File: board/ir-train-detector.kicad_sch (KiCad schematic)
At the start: 21 parts, among them J1 Conn_01x03

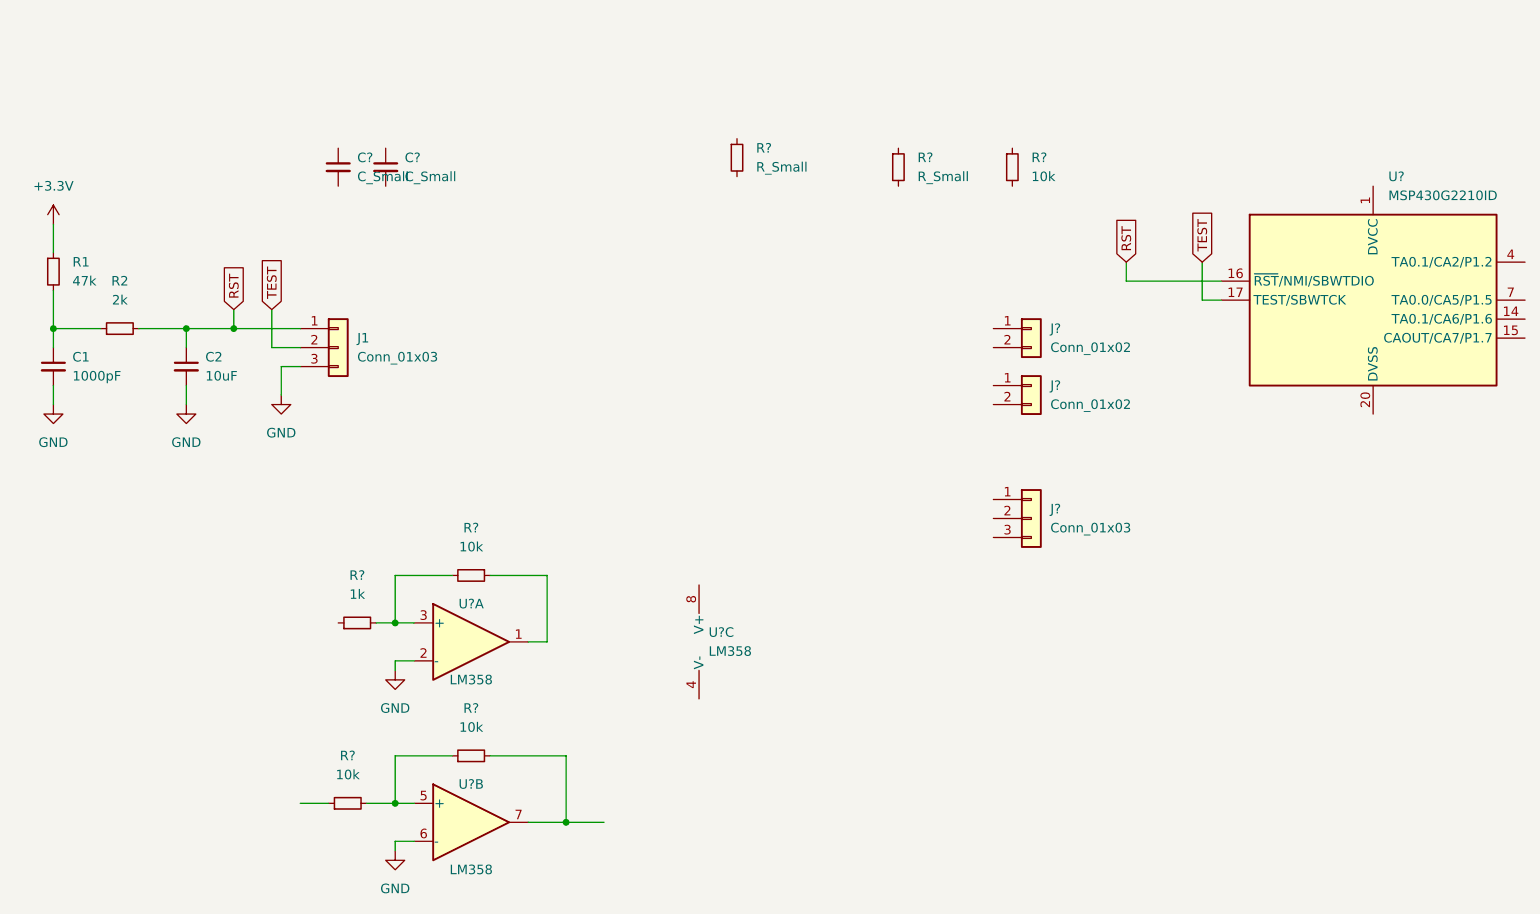
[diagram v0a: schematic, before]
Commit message: power section schematic finished
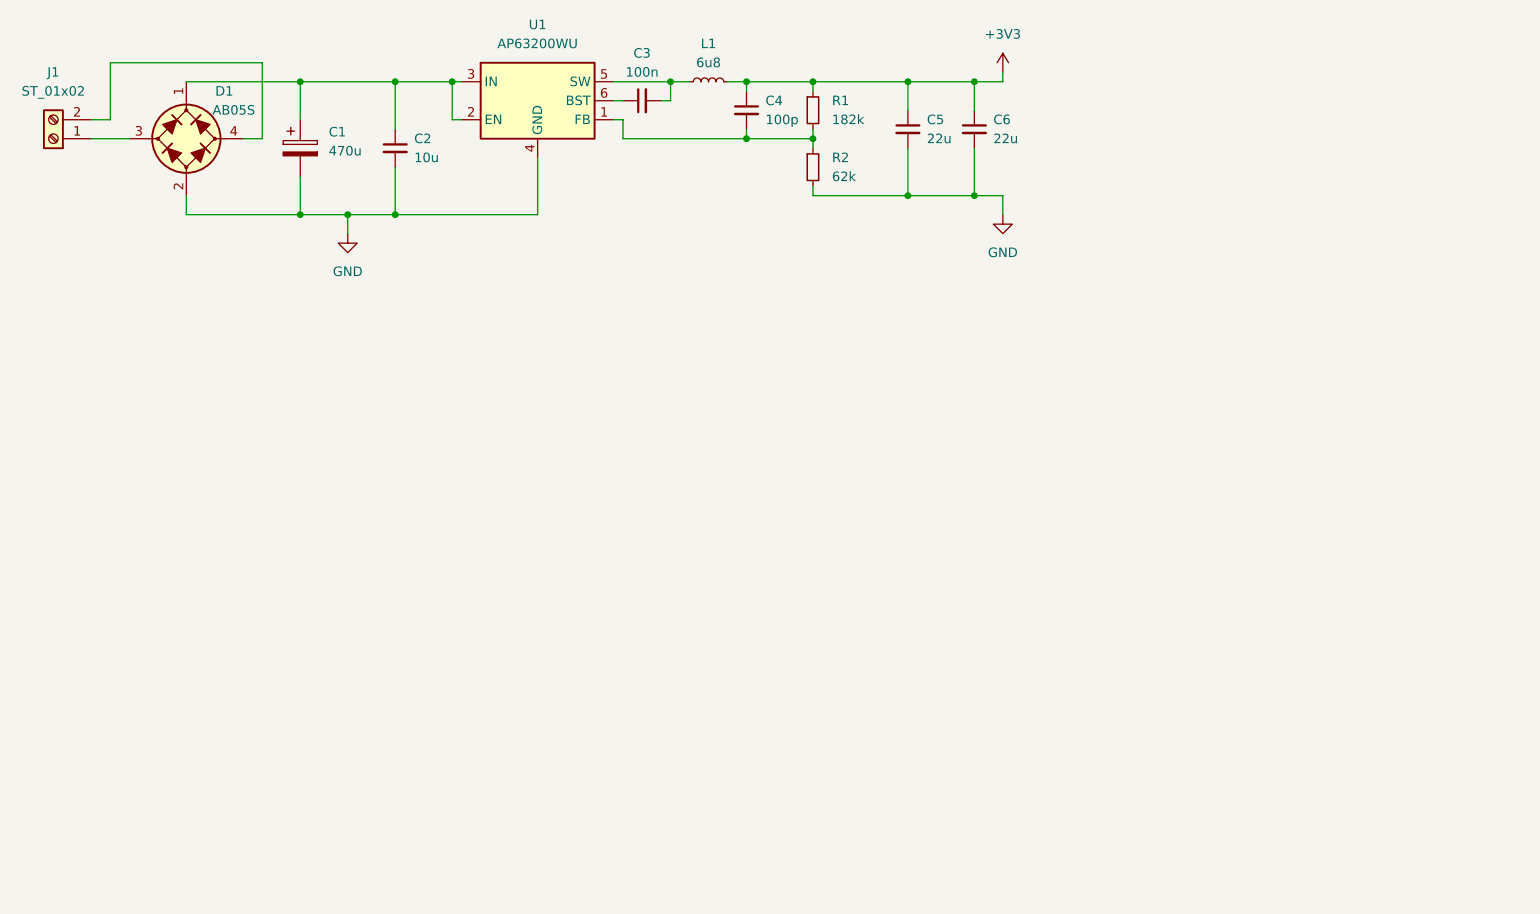
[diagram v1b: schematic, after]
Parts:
- removed C1: 1000pF, Capacitor_SMD:C_0805_2012Metric_Pad1.18x1.45mm_HandSolder, symbol Device:C_Small
- removed C? (x2): C_Small, symbol Device:C_Small
- removed J1: Conn_01x03, Connector_PinHeader_2.54mm:PinHeader_1x03_P2.54mm_Vertical, symbol Connector_Generic:Conn_01x03
- removed J? (x2): Conn_01x02, symbol Connector_Generic:Conn_01x02
- removed J?: Conn_01x03, symbol Connector_Generic:Conn_01x03
- removed R? (x3): 10k, Resistor_SMD:R_0805_2012Metric_Pad1.20x1.40mm_HandSolder, symbol Device:R_Small
- removed R?: 10k, symbol Device:R_Small
- removed R? (x2): R_Small, symbol Device:R_Small
- removed R?: 1k, Resistor_SMD:R_0805_2012Metric_Pad1.20x1.40mm_HandSolder, symbol Device:R_Small
- removed U? (x3): LM358, symbol Amplifier_Operational:LM358
- removed U?: MSP430G2210ID, Package_SO:SOIC-8_3.9x4.9mm_P1.27mm, symbol MCU_Texas_MSP430:MSP430G2210ID
- added C1: 470u, Capacitor_THT_AKL:CP_Radial_D12.5mm_P5.00mm, symbol Capacitor_AKL:CP_Radial_D12.5mm_P5.00mm
- added C3: 100n, Capacitor_SMD:C_0603_1608Metric_Pad1.08x0.95mm_HandSolder, symbol Device:C_Small
- added C4: 100p, Capacitor_SMD:C_0603_1608Metric_Pad1.08x0.95mm_HandSolder, symbol Device:C_Small
- added C5, C6: 22u, Capacitor_SMD:C_0805_2012Metric_Pad1.18x1.45mm_HandSolder, symbol Device:C_Small
- added D1: AB05S, Diode_SMD_AKL:Diode_Bridge_Diotec_ABS, symbol Diode_Bridge_AKL:AB05S
- added J1: ST_01x02, symbol Connector:Screw_Terminal_01x02
- added L1: 6u8, symbol Device:L_Small
- added U1: AP63200WU, Package_TO_SOT_SMD:TSOT-23-6, symbol Regulator_Switching:AP63200WU
- C2: value 10uF -> 10u; footprint Capacitor_SMD:C_0805_2012Metric_Pad1.18x1.45mm_HandSolder -> Capacitor_SMD:C_1206_3216Metric_Pad1.33x1.80mm_HandSolder
- R1: value 47k -> 182k; footprint Resistor_SMD:R_0805_2012Metric_Pad1.20x1.40mm_HandSolder -> Resistor_SMD:R_0603_1608Metric_Pad0.98x0.95mm_HandSolder
- R2: value 2k -> 62k; footprint Resistor_SMD:R_0805_2012Metric_Pad1.20x1.40mm_HandSolder -> Resistor_SMD:R_0603_1608Metric_Pad0.98x0.95mm_HandSolder
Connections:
- net GND: now also R2.2, C1.2, C5.2, C6.2, D1.2 (-), U1.4 (GND)
- net at R1.2, R2.1: now also C4.2, U1.1 (FB)
- net +3.3V renamed +3V3
- net +3V3: now also C4.1, C5.1, C6.1, L1.2
- net RST: no longer names the net of C2.1
- net RST: now also C1.1, D1.1 (+), U1.2 (EN), U1.3 (IN); no longer R2.2
- new net: D1.3 (1), J1.1 (Pin_1)
- new net: D1.4 (2), J1.2 (Pin_2)
- new net: C3.1, U1.6 (BST)
- new net: C3.2, L1.1, U1.5 (SW)

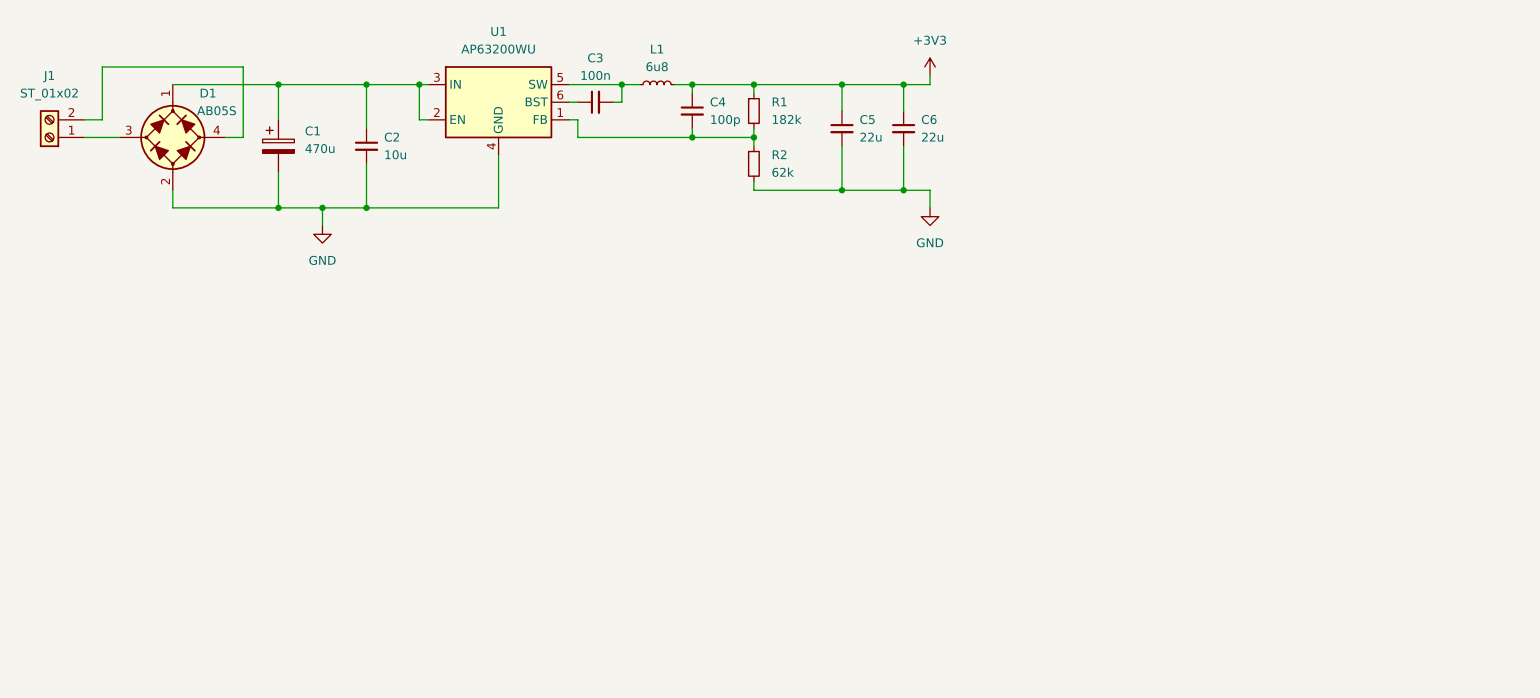
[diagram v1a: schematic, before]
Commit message: added usb interface
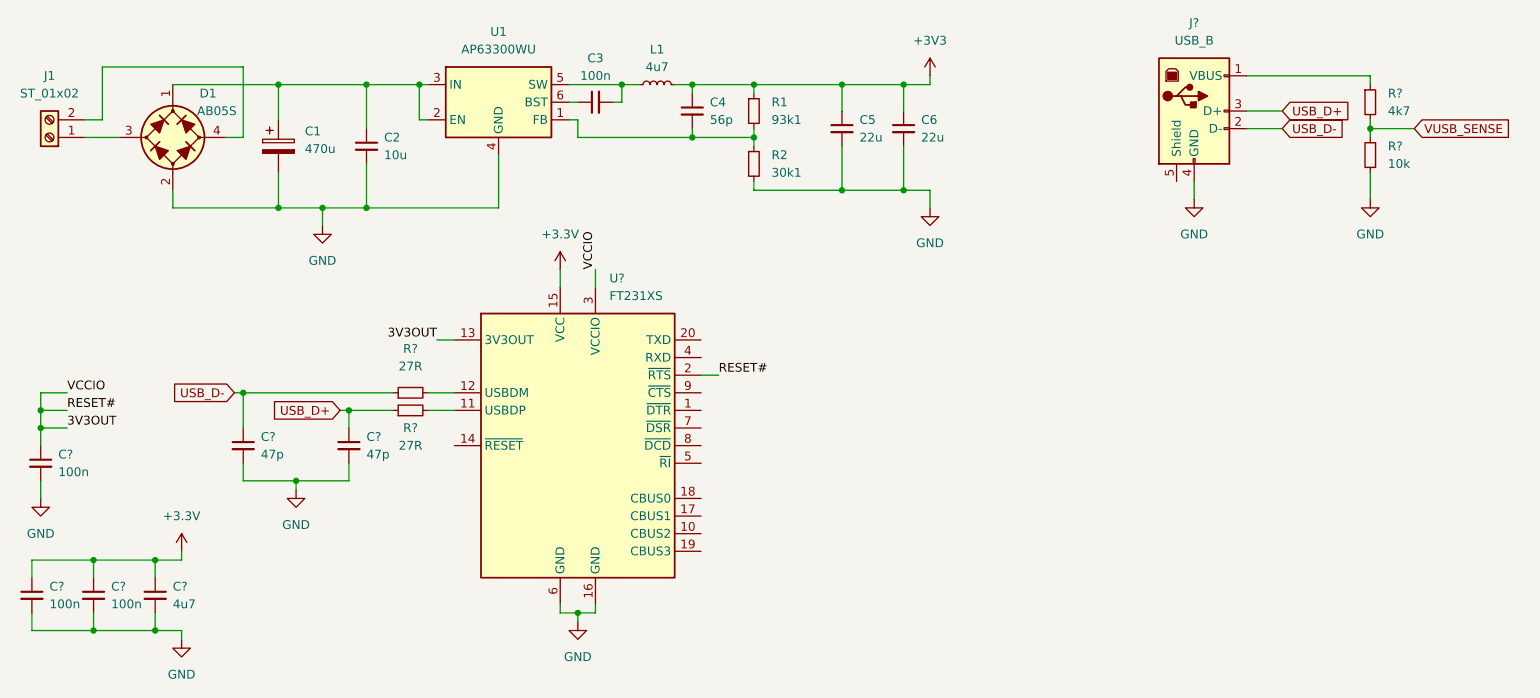
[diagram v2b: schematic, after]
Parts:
- added C?: 4u7, symbol Device:C_Small
- added C? (x2): 47p, symbol Device:C_Small
- added C? (x3): 100n, symbol Device:C_Small
- added J?: USB_B, Connector_USB:USB_B_Lumberg_2411_02_Horizontal, symbol Connector:USB_B
- added R?: 10k, symbol Device:R_Small
- added R? (x2): 27R, symbol Device:R_Small
- added R?: 4k7, symbol Device:R_Small
- added U?: FT231XS, Package_SO:SSOP-20_3.9x8.7mm_P0.635mm, symbol Interface_USB:FT231XS
- C1: footprint Capacitor_THT_AKL:CP_Radial_D12.5mm_P5.00mm -> (none)
- C2: footprint Capacitor_SMD:C_1206_3216Metric_Pad1.33x1.80mm_HandSolder -> (none)
- C3: footprint Capacitor_SMD:C_0603_1608Metric_Pad1.08x0.95mm_HandSolder -> (none)
- C4: value 100p -> 56p; footprint Capacitor_SMD:C_0603_1608Metric_Pad1.08x0.95mm_HandSolder -> (none)
- C5, C6: footprint Capacitor_SMD:C_0805_2012Metric_Pad1.18x1.45mm_HandSolder -> (none)
- D1: footprint Diode_SMD_AKL:Diode_Bridge_Diotec_ABS -> (none)
- L1: value 6u8 -> 4u7
- R1: value 182k -> 93k1; footprint Resistor_SMD:R_0603_1608Metric_Pad0.98x0.95mm_HandSolder -> (none)
- R2: value 62k -> 30k1; footprint Resistor_SMD:R_0603_1608Metric_Pad0.98x0.95mm_HandSolder -> (none)
- U1: value AP63200WU -> AP63300WU; footprint Package_TO_SOT_SMD:TSOT-23-6 -> (none)
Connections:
- net +3V3: now also C?.1, C?.1, C?.1, U?.15 (VCC)
- net GND: now also C?.2, C?.2, C?.2, C?.2, C?.2, C?.2, J?.4 (GND), R?.1, U?.16 (GND), U?.6 (GND)
- new net: J?.1 (VBUS), R?.1
- new net: R?.2, U?.11 (USBDP)
- new net: R?.2, U?.12 (USBDM)
- new net 3V3OUT: C?.1, U?.13 (3V3OUT), U?.2 (~{RTS}), U?.3 (VCCIO)
- new net USB_D+: C?.1, J?.3 (D+), R?.1
- new net USB_D-: C?.1, J?.2 (D-), R?.1
- new net VUSB_SENSE: R?.2, R?.2

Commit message: first draft of final schematic
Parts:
- added C? (x5): 16n, symbol Device:C_Small
- added C? (x3): 100n, symbol Device:C_Small
- added C?: 2n2, symbol Device:C_Small
- added C?: 10u, symbol Device:C_Small
- added D? (x6): LED, symbol Device:LED
- added J?: Conn_01x07, symbol Connector_Generic:Conn_01x07
- added J?: JTAG, symbol Connector_Generic:Conn_02x07_Odd_Even
- added J? (x5): IR_MOD1, symbol Connector_Generic:Conn_01x03
- added J?: BSL_SEL, symbol Connector_Generic:Conn_01x03
- added Q? (x5): AO3407A, Package_TO_SOT_SMD_AKL:SOT-23, symbol Transistor_MOSFET_AKL:AO3407A
- added R? (x5): 10k, symbol Device:R_Small
- added R? (x5): 470k, symbol Device:R_Small
- added R? (x7): 100k, symbol Device:R_Small
- added R? (x5): 18R, symbol Device:R_Small
- added R? (x6): 220R, symbol Device:R_Small
- added R?: 47k, symbol Device:R_Small
- added R?: 330R, symbol Device:R_Small
- added U? (x3): LM358, 4ms_Package_SSOP:TSSOP-8_4.4x3mm_Pitch0.65mm, symbol 4ms_IC:LM358
- added U? (x5): LM324A, symbol Amplifier_Operational:LM324A
- added U?: MSP430G2553IPW28, Package_SO:TSSOP-28_4.4x9.7mm_P0.65mm, symbol MCU_Texas_MSP430:MSP430G2553IPW28
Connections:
- net +3V3: now also C?.1, C?.1, C?.1, C?.1, J?.1 (Pin_1), J?.4 (Pin_4), Q?.2 (S), Q?.2 (S), Q?.2 (S), Q?.2 (S), Q?.2 (S), R?.1, R?.1, R?.1, R?.1, R?.1, R?.1, R?.1, R?.2, U?.1 (DVCC), U?.4 (V+), U?.8 (V+)
- net 3V3OUT: now also U?.14 (~{RESET}); no longer U?.2 (~{RTS})
- net GND: now also C?.2, C?.2, C?.2, C?.2, C?.2, D?.1 (K), D?.1 (K), D?.1 (K), D?.1 (K), D?.1 (K), J?.2 (Pin_2), J?.2 (Pin_2), J?.2 (Pin_2), J?.2 (Pin_2), J?.2 (Pin_2), J?.7 (Pin_7), J?.9 (Pin_9), R?.1, R?.1, R?.1, R?.1, R?.1, R?.2, U?.11 (V-), U?.13 (-), U?.2 (-), U?.2 (-), U?.28 (DVSS), U?.4 (V-), U?.6 (-), U?.9 (-)
- net VUSB_SENSE: now also U?.10 (CBUS2)
- net FT231_DTR#: now reaches U?.1 (~{DTR})
- net FT231_DTR#: now also C?.1, J?.1 (Pin_1), R?.2, U?.24 (~{RST}/NMI/SBWTDIO)
- net at U?.19 (CBUS3): now also D?.1 (K)
- net FT231_TX: now reaches U?.20 (TXD)
- net FT231_TX: now also U?.3 (TA0.0/UCA0RXD/UCA0SOMI/A1/CA1/P1.1)
- net FT231_RX: now reaches U?.4 (RXD)
- net FT231_RX: now also J?.2 (Pin_2)
- new net: C?.1, R?.2, U?.8
- new net: D?.2 (A), R?.1 (x6)
- new net: Q?.3 (D), R?.1 (x5)
- new net: J?.1 (Pin_1), R?.1, U?.3 (+) (x2)
- new net: C?.1, R?.2, U?.1 (x2)
- new net: J?.3 (Pin_3), R?.2 (x5)
- new net: J?.1 (Pin_1), R?.1, U?.10 (+)
- new net: J?.1 (Pin_1), R?.1, U?.12 (+)
- new net: C?.1, R?.2, U?.14
- new net: R?.1, R?.2, U?.5 (+)
- new net: J?.1 (Pin_1), R?.1, U?.5 (+)
- new net: U?.6 (-), U?.7
- new net: C?.1, R?.2, U?.7
- new net FT231_RTS#: J?.8 (Pin_8), R?.1, U?.2 (~{RTS}), U?.25 (SBWTCK/TEST)
- new net MODULE1_IN: C?.2, R?.2, U?.5 (ADC10CLK/CAOUT/VREF-/VeREF-/A3/CA3/P1.3)
- new net MODULE1_OUT: Q?.1 (G), R?.2, U?.10 (TA1.0/P2.0)
- new net MODULE1_STATUS: J?.2 (Pin_2), R?.2, U?.9 (P3.0/TA0.2)
- new net MODULE2_IN: C?.2, R?.2, U?.6 (TCK/SMCLK/UCB0STE/UCA0CLK/VREF+/VeREF+/A4/CA4/P1.4)
- new net MODULE2_OUT: Q?.1 (G), R?.2, U?.11 (TA1.1/P2.1)
- new net MODULE2_STATUS: J?.3 (Pin_3), R?.2, U?.8 (P3.1/TA1.0)
- new net MODULE3_IN: C?.2, R?.2, U?.7 (TMS/TA0.0/UCB0CLK/UCA0STE/A5/CA5/P1.5)
- new net MODULE3_OUT: Q?.1 (G), R?.2, U?.12 (TA1.1/P2.2)
- new net MODULE3_STATUS: J?.4 (Pin_4), R?.2, U?.13 (P3.2/TA1.1)
- new net MODULE4_IN: C?.2, R?.2, U?.22 (TDI/TCLK/TA0.1/UCB0SOMI/UCB0SCL/A6/CA6/P1.6)
- new net MODULE4_OUT: Q?.1 (G), R?.2, U?.16 (TA1.0/P2.3)
- new net MODULE4_STATUS: J?.5 (Pin_5), R?.2, U?.14 (P3.3/TA1.2)
- new net MODULE5_IN: C?.2, R?.2, U?.23 (TDO/TDI/CAOUT/UCB0SIMO/UCB0SDA/A7/CA7/P1.7)
- new net MODULE5_OUT: Q?.1 (G), R?.2, U?.17 (TA1.2/P2.4)
- new net MODULE5_STATUS: J?.6 (Pin_6), R?.2, U?.15 (P3.4/TA0.0)
- new net MSP_BSL_TX: J?.3 (Pin_3)
- new net MSP_UART_TX: J?.1 (Pin_1), U?.4 (TA0.1/UCA0TXD/UCA0SIMO/A2/CA2/P1.2)
- new net TCK: J?.7 (Pin_7), R?.2
- no-connect marks 0 -> 23
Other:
- moved on the sheet: J?, R?, U?

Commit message: added footprints
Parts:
- removed Q? (x4): AO3407A, Package_TO_SOT_SMD_AKL:SOT-23, symbol Transistor_MOSFET_AKL:AO3407A
- removed R? (x4): 100k, symbol Device:R_Small
- added Q1, Q3, Q4, Q5: AO3407A, Package_TO_SOT_SMD_AKL:SOT-23, symbol Transistor_MOSFET_AKL:AO3407A
- added R17, R19, R20, R21, R37: 470R, symbol Device:R_Small
- added R38, R39, R40, R41: 10k, symbol Device:R_Small
- C1: footprint (none) -> Capacitor_THT:CP_Radial_D12.5mm_P5.00mm
- C10, C11, C12, C15, C16, C17, C7, C8: renamed from C?; footprint (none) -> Capacitor_SMD_Handsoldering_AKL:C_0603_1608Metric
- C13, C14: renamed from C?; footprint (none) -> Capacitor_SMD_Handsoldering_AKL:C_0805_2012Metric
- C18, C19, C20, C21, C22: renamed from C?; value 16n -> 33n; footprint (none) -> Capacitor_SMD_Handsoldering_AKL:C_0603_1608Metric
- C2: footprint (none) -> Capacitor_SMD_Handsoldering_AKL:C_1206_3216Metric
- C3, C4: footprint (none) -> Capacitor_SMD_Handsoldering_AKL:C_0603_1608Metric
- C5, C6: footprint (none) -> Capacitor_SMD_Handsoldering_AKL:C_0805_2012Metric
- C9: renamed from C?; footprint (none) -> Capacitor_SMD_Handsoldering_AKL:C_1206_3216Metric
- D1: footprint (none) -> Diode_SMD_Handsoldering_AKL:Diode_Bridge_Diotec_ABS
- D2, D3, D4, D5, D6, D7: renamed from D?; footprint (none) -> LED_SMD:LED_0603_1608Metric_Pad1.05x0.95mm_HandSolder
- L1: footprint (none) -> Inductor_SMD_Handsoldering_AKL:L_7.3x7.3_H4.5
- R1, R2: footprint (none) -> Resistor_SMD_AKL:R_0603_1608Metric_Pad1.05x0.95mm_HandSolder
- R10, R11, R3, R4, R5, R9: renamed from R?; footprint (none) -> Resistor_SMD_AKL:R_0603_1608Metric_Pad1.05x0.95mm_HandSolder
- R12, R13, R14, R15, R16, R6: renamed from R?; value 220R -> 330R; footprint (none) -> Resistor_SMD_AKL:R_0603_1608Metric_Pad1.05x0.95mm_HandSolder
- R18: renamed from R?; value 100k -> 10k
- R7, R8: renamed from R?; value 100k -> 10k; footprint (none) -> Resistor_SMD_AKL:R_0603_1608Metric_Pad1.05x0.95mm_HandSolder
- U5: renamed from U?; footprint (none) -> Package_SO_AKL:SOIC-14_3.9x8.7mm_P1.27mm
- gave numbers to parts that had none: 28
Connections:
- net +3V3: now also Q1.2 (S), Q3.2 (S), Q4.2 (S), Q5.2 (S), R38.1, R39.1, R40.1, R41.1
- net MODULE1_OUT: now also R19.1; no longer Q2.1 (G), R18.2
- net MODULE2_OUT: now also R20.1
- net MODULE3_OUT: now also R21.1
- net MODULE4_OUT: now also R37.1
- net MODULE5_OUT: now also R17.1
- net at R26.1: now also Q5.3 (D)
- net at R25.1: now also Q4.3 (D)
- net at R24.1: now also Q3.3 (D)
- net at R22.1: now also Q1.3 (D)
- new net: Q5.1 (G), R37.2, R41.2
- new net: Q4.1 (G), R21.2, R40.2
- new net: Q2.1 (G), R18.2, R19.2
- new net: Q1.1 (G), R17.2, R38.2
- new net: Q3.1 (G), R20.2, R39.2
